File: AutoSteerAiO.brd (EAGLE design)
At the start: 114.3 x 99.1 mm, 84 parts, among them IC2 MMA8452Q, J4 CONNECTOR 1x5 PINS, K4 CB1A-P-12V, U1 VX7805-1000

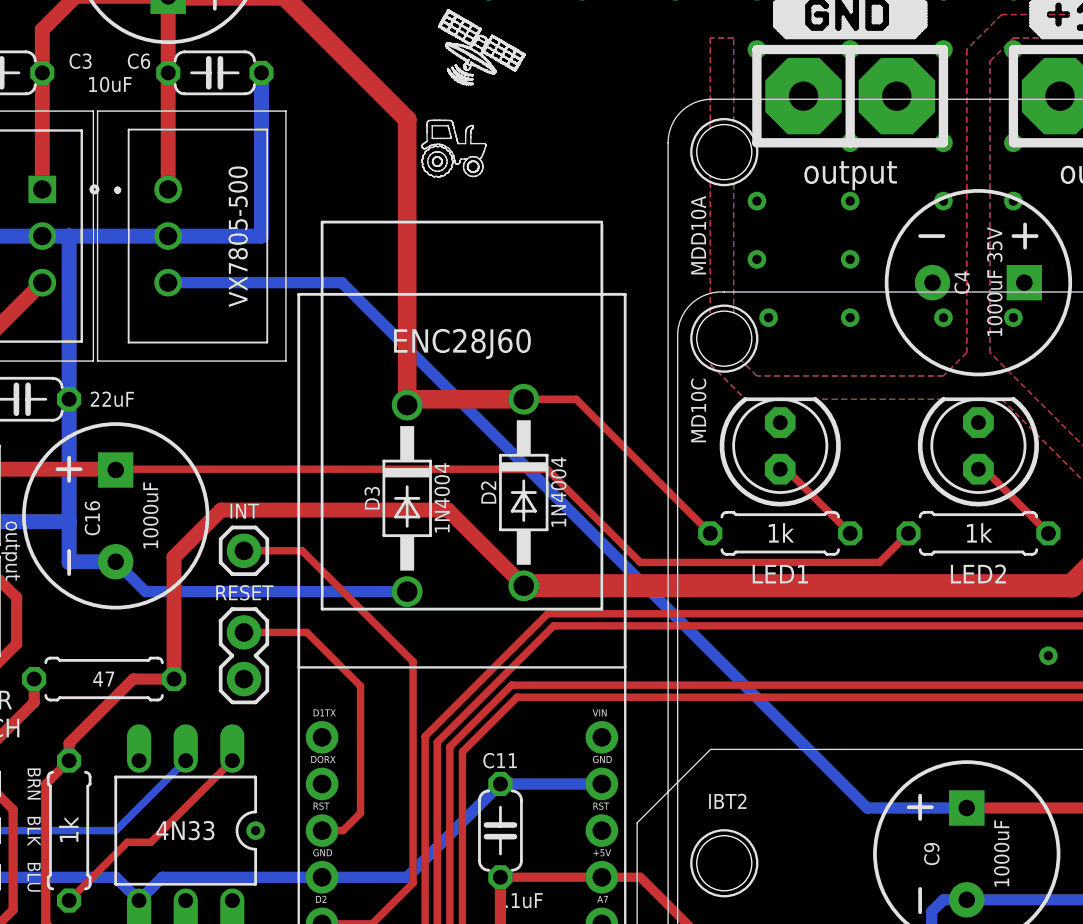
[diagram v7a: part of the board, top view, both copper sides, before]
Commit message: Add files via upload
edit silkscreen
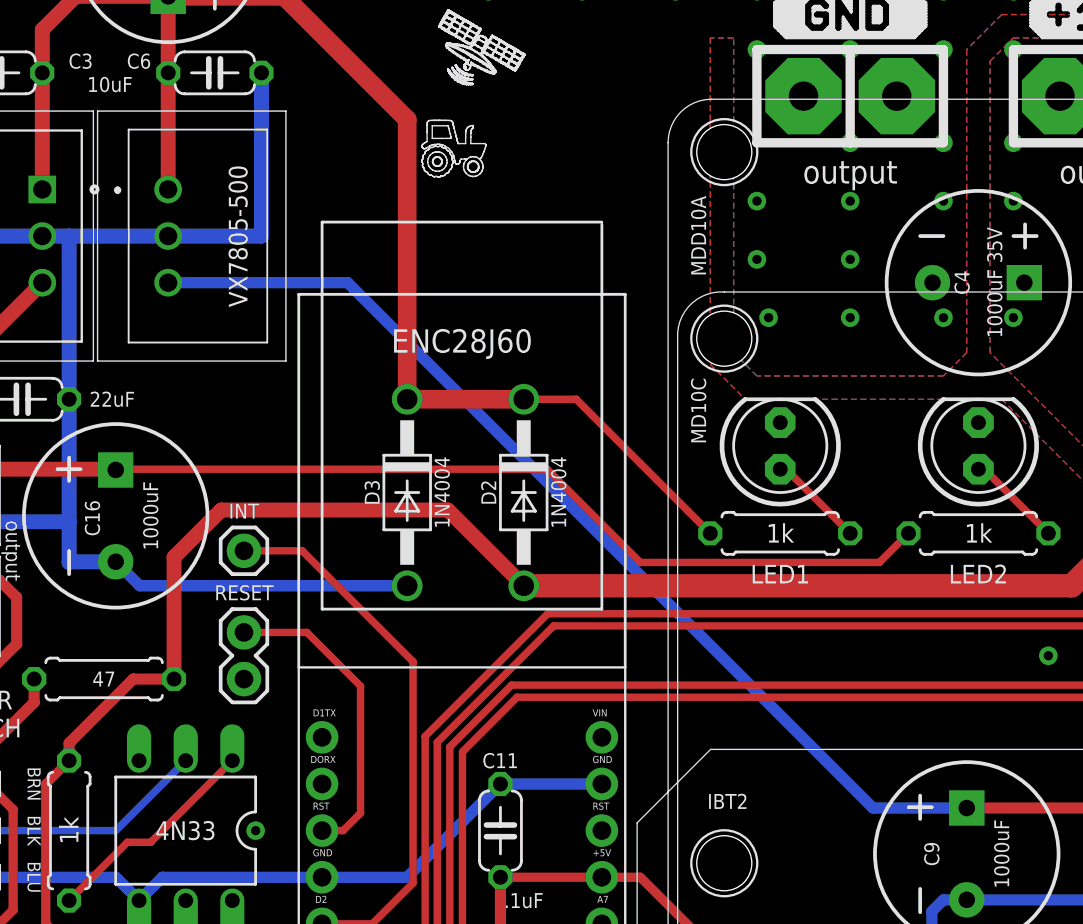
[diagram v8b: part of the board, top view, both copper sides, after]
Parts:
- moved D3 0.32 mm to (28.6, 63.5)
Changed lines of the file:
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@@
 <drawing>
 <settings>
-<setting alwaysvectorfont="yes"/>
+<setting alwaysvectorfont="no"/>
 <setting keepoldvectorfont="yes"/>
 <setting verticaltext="up"/>
@@
 <attribute name="CYTRON-PC" value="CN-2600PS-05" x="109.855" y="48.26" size="1.778" layer="27" rot="R90" display="off"/>
 <attribute name="DESC" value="2600 PCB Connector" x="109.855" y="48.26" size="1.778" layer="27" rot="R90" display="off"/>
-<attribute name="LABEL" value="" x="112.776" y="46.863" size="0.762" layer="21" font="vector" ratio="15" rot="R90" align="top-left"/>
 <attribute name="LABEL" value="" x="112.776" y="46.863" size="0.762" layer="51" font="vector" ratio="15" rot="R90" align="top-left"/>
+<attribute name="LABEL" value="" x="112.776" y="46.863" size="0.762" layer="21" font="vector" ratio="15" rot="R90" align="top-left"/>
 <attribute name="LABEL" value="" x="109.855" y="48.26" size="1.778" layer="27" rot="R90" display="off"/>
 <attribute name="MF" value="" x="109.855" y="48.26" size="1.778" layer="27" rot="R90" display="off"/>
@@
 <attribute name="VALUE" x="36.83" y="63.5" size="0.8128" layer="25" font="vector" ratio="12" rot="R90" align="center"/>
 </element>
-<element name="D3" library="diode" library_urn="urn:adsk.eagle:library:210" package="DO41-10" package3d_urn="urn:adsk.eagle:package:43336/1" value="1N4004" x="28.575" y="63.1825" smashed="yes" rot="R270">
-<attribute name="MF" value="" x="28.575" y="63.1825" size="1.778" layer="27" rot="R270" display="off"/>
-<attribute name="MPN" value="" x="28.575" y="63.1825" size="1.778" layer="27" rot="R270" display="off"/>
-<attribute name="NAME" x="26.67" y="63.1825" size="0.8128" layer="25" font="vector" ratio="12" rot="R270" align="center"/>
-<attribute name="OC_NEWARK" value="unknown" x="28.575" y="63.1825" size="1.778" layer="27" rot="R270" display="off"/>
-<attribute name="VALUE" x="30.48" y="63.1825" size="0.8128" layer="25" font="vector" ratio="12" rot="R270" align="center"/>
+<element name="D3" library="diode" library_urn="urn:adsk.eagle:library:210" package="DO41-10" package3d_urn="urn:adsk.eagle:package:43336/1" value="1N4004" x="28.575" y="63.5" smashed="yes" rot="R270">
+<attribute name="MF" value="" x="28.575" y="63.5" size="1.778" layer="27" rot="R270" display="off"/>
+<attribute name="MPN" value="" x="28.575" y="63.5" size="1.778" layer="27" rot="R270" display="off"/>
+<attribute name="NAME" x="26.67" y="63.5" size="0.8128" layer="25" font="vector" ratio="12" rot="R270" align="center"/>
+<attribute name="OC_NEWARK" value="unknown" x="28.575" y="63.5" size="1.778" layer="27" rot="R270" display="off"/>
+<attribute name="VALUE" x="30.48" y="63.5" size="0.8128" layer="25" font="vector" ratio="12" rot="R270" align="center"/>
 </element>
 <element name="R4" library="resistor" library_urn="urn:adsk.eagle:library:348" package="0207/7" package3d_urn="urn:adsk.eagle:package:23493/2" value="330" x="96.52" y="20.955" smashed="yes" rot="R180">
@@
 <via x="105.41" y="2.54" extent="1-16" drill="0.508"/>
 <via x="33.02" y="90.805" extent="1-16" drill="0.508"/>
-<wire x1="28.575" y1="58.1025" x2="14.3275" y2="58.1025" width="0.6096" layer="16"/>
-<wire x1="12.7" y1="59.73" x2="14.3275" y2="58.1025" width="0.6096" layer="16"/>
+<wire x1="28.575" y1="58.42" x2="14.01" y2="58.42" width="0.6096" layer="16"/>
+<wire x1="12.7" y1="59.73" x2="14.01" y2="58.42" width="0.6096" layer="16"/>
 <polygon width="0" layer="1" isolate="0.3556" thermals="no" rank="2">
 <vertex x="46.99" y="68.58"/>
@@
 <wire x1="8.6995" y1="86.36" x2="8.7" y2="86.3595" width="0.8128" layer="1"/>
 <wire x1="8.7" y1="86.3595" x2="8.7" y2="80.01" width="0.8128" layer="1"/>
-<wire x1="34.925" y1="68.58" x2="28.8925" y2="68.58" width="1.016" layer="1"/>
-<wire x1="28.575" y1="68.2625" x2="28.8925" y2="68.58" width="1.016" layer="1"/>
-<wire x1="28.575" y1="68.2625" x2="28.575" y2="83.82" width="1.016" layer="1"/>
+<wire x1="34.925" y1="68.58" x2="28.575" y2="68.58" width="1.016" layer="1"/>
+<wire x1="28.575" y1="68.58" x2="28.575" y2="83.82" width="1.016" layer="1"/>
 <wire x1="21.8675" y1="90.5275" x2="15.5575" y2="90.5275" width="1.016" layer="1"/>
 <wire x1="28.575" y1="83.82" x2="21.8675" y2="90.5275" width="1.016" layer="1"/>
@@
 <wire x1="67.31" y1="45.72" x2="66.715" y2="46.315" width="0.6096" layer="1"/>
 <wire x1="66.715" y1="46.315" x2="59.055" y2="46.315" width="0.6096" layer="1"/>
-<wire x1="53.629" y1="46.315" x2="25.014" y2="74.93" width="0.6096" layer="16"/>
-<wire x1="15.5525" y1="74.93" x2="25.014" y2="74.93" width="0.6096" layer="16"/>
-<wire x1="53.629" y1="46.315" x2="59.055" y2="46.315" width="0.6096" layer="16"/>
+<wire x1="53.9465" y1="46.315" x2="25.3315" y2="74.93" width="0.6096" layer="16"/>
+<wire x1="15.5525" y1="74.93" x2="25.3315" y2="74.93" width="0.6096" layer="16"/>
+<wire x1="53.9465" y1="46.315" x2="59.055" y2="46.315" width="0.6096" layer="16"/>
 </signal>
 <signal name="N$3">
